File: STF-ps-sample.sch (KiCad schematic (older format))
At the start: 69 parts

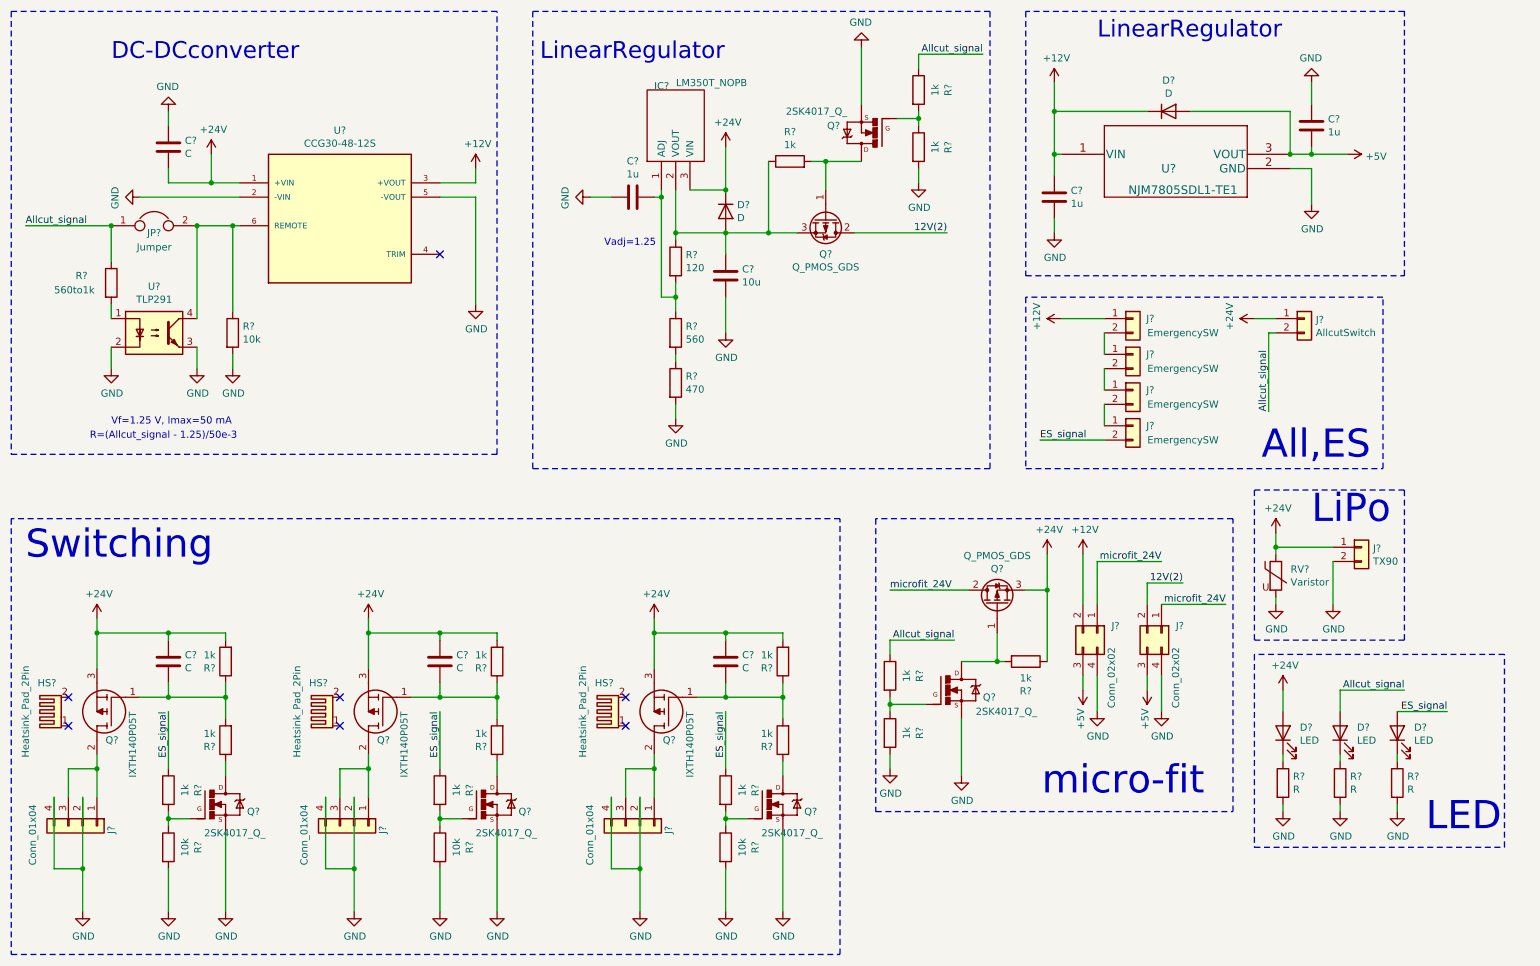
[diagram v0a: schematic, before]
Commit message: just started pcb layout
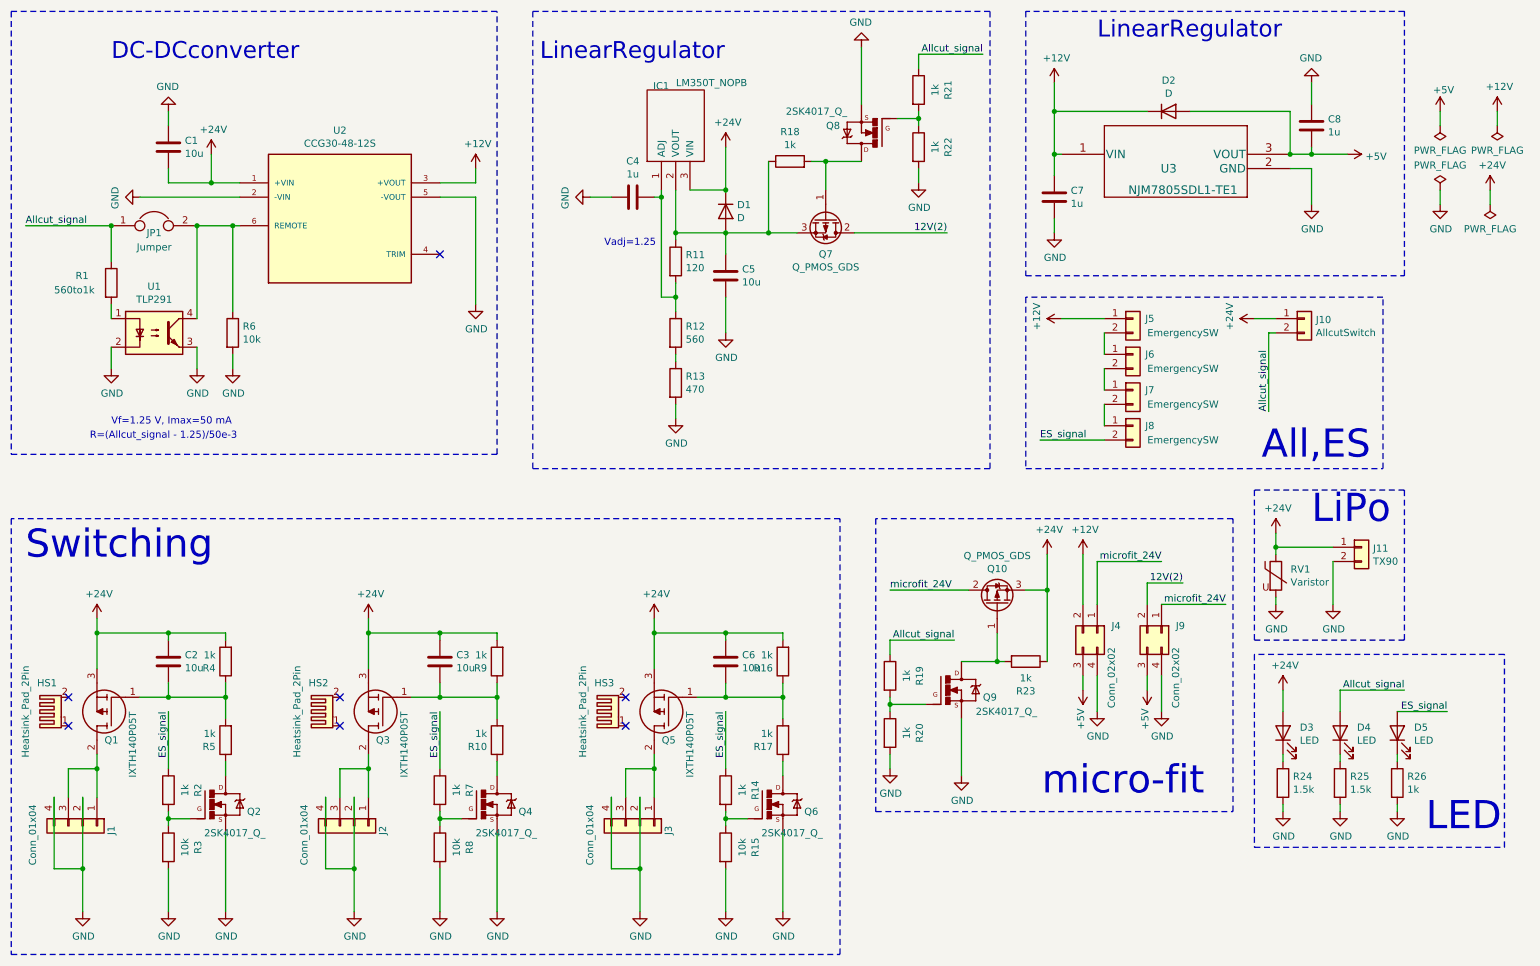
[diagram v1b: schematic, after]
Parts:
- C1, C2, C3, C6: renamed from C?; value C -> 10u; footprint (none) -> Capacitor_THT:C_Disc_D4.3mm_W1.9mm_P5.00mm
- C4, C5, C7, C8: renamed from C?; footprint (none) -> Capacitor_THT:C_Disc_D4.3mm_W1.9mm_P5.00mm
- D1, D2: renamed from D?; footprint (none) -> Diode_THT:D_DO-35_SOD27_P2.54mm_Vertical_AnodeUp
- D3, D4, D5: renamed from D?; footprint (none) -> LED_THT:LED_D3.0mm
- HS1, HS2, HS3: renamed from HS?; footprint (none) -> 00_kicad_mods:stf_01_HeatSink_25x17
- IC1: renamed from IC?; footprint TO254P470X1028X1955-3P -> 00_kicad_mods:stf_03_LM350T
- J1, J2, J3: renamed from J?; footprint (none) -> 00_kicad_mods:stf_08_tanshidai_4P_cover
- J10, J5, J6, J7, J8: renamed from J?; footprint (none) -> Connector_JST:JST_XH_B2B-XH-A_1x02_P2.50mm_Vertical
- J11: renamed from J?; footprint (none) -> 00_kicad_mods:stf_06_XT90PW
- J4, J9: renamed from J?; footprint (none) -> 00_kicad_mods:stf_07_molex_microfit4P_vertical_3Dmodel
- JP1: renamed from JP?; footprint (none) -> Jumper:SolderJumper-2_P1.3mm_Open_TrianglePad1.0x1.5mm
- Q1, Q3, Q5: renamed from Q?; footprint TO545P530X1600X2596-3P -> 00_kicad_mods:stf_02_IXTH140P05T
- Q10, Q7: renamed from Q?; footprint (none) -> 00_kicad_mods:stf_11_TO230P230X650X740-3P
- Q2, Q4, Q6, Q8, Q9: renamed from Q?; footprint TO230P230X650X740-3P -> 00_kicad_mods:stf_11_TO230P230X650X740-3P
- R1, R10, R11, R12, R13, R14, R15, R16, R17, R18, R19, R2, R20, R21, R22, R23, R3, R4, R5, R6, R7, R8, R9: renamed from R?; footprint (none) -> Resistor_THT:R_Axial_DIN0204_L3.6mm_D1.6mm_P5.08mm_Horizontal
- R24, R25: renamed from R?; value R -> 1.5k; footprint (none) -> Resistor_THT:R_Axial_DIN0204_L3.6mm_D1.6mm_P5.08mm_Horizontal
- R26: renamed from R?; value R -> 1k; footprint (none) -> Resistor_THT:R_Axial_DIN0204_L3.6mm_D1.6mm_P5.08mm_Horizontal
- RV1: renamed from RV?; footprint (none) -> Varistor:RV_Disc_D9mm_W3.3mm_P5mm
- U1: renamed from U?; footprint Package_SO:SOIC-4_4.55x2.6mm_P1.27mm -> 00_kicad_mods:stf_05_TLP291_4.55x2.6mm_P1.27mm
- U2: renamed from U?; footprint CCG30-48-12S -> 00_kicad_mods:stf_09_CCG30-48-12S
- U3: renamed from U?; footprint TO-252-3-L1_NMD -> 00_kicad_mods:stf_04_NJM7805SDL1-TE1

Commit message: fnished
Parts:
- R1, R19: footprint Resistor_THT:R_Axial_DIN0204_L3.6mm_D1.6mm_P5.08mm_Horizontal -> Resistor_THT:R_Axial_DIN0204_L3.6mm_D1.6mm_P7.62mm_Horizontal
- R14, R7: footprint Resistor_THT:R_Axial_DIN0204_L3.6mm_D1.6mm_P5.08mm_Horizontal -> Resistor_THT:R_Axial_DIN0207_L6.3mm_D2.5mm_P10.16mm_Horizontal
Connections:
- net ES_signal: now also R26.1; no longer D5.2 (A)
- net GND: now also D5.1 (K); no longer R26.2
- new net: D5.2 (A), R26.2
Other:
- moved on the sheet: D5, R26
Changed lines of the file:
@@
 F 0 "R1" H 1050 2600 50  0000 L CNN
 F 1 "560to1k" H 900 2500 50  0000 L CNN
-F 2 "Resistor_THT:R_Axial_DIN0204_L3.6mm_D1.6mm_P5.08mm_Horizontal" V 1230 2550 50  0001 C CNN
+F 2 "Resistor_THT:R_Axial_DIN0204_L3.6mm_D1.6mm_P7.62mm_Horizontal" V 1230 2550 50  0001 C CNN
 F 3 "~" H 1300 2550 50  0001 C CNN
 	1    1300 2550
@@
 F 0 "R7" V 3807 6100 50  0000 C CNN
 F 1 "1k" V 3716 6100 50  0000 C CNN
-F 2 "Resistor_THT:R_Axial_DIN0204_L3.6mm_D1.6mm_P5.08mm_Horizontal" V 3530 6100 50  0001 C CNN
+F 2 "Resistor_THT:R_Axial_DIN0207_L6.3mm_D2.5mm_P10.16mm_Horizontal" V 3530 6100 50  0001 C CNN
 F 3 "~" H 3600 6100 50  0001 C CNN
 	1    3600 6100
@@
 F 0 "R14" V 5807 6100 50  0000 C CNN
 F 1 "1k" V 5716 6100 50  0000 C CNN
-F 2 "Resistor_THT:R_Axial_DIN0204_L3.6mm_D1.6mm_P5.08mm_Horizontal" V 5530 6100 50  0001 C CNN
+F 2 "Resistor_THT:R_Axial_DIN0207_L6.3mm_D2.5mm_P10.16mm_Horizontal" V 5530 6100 50  0001 C CNN
 F 3 "~" H 5600 6100 50  0001 C CNN
 	1    5600 6100
@@
 F 0 "R19" V 6957 5300 50  0000 C CNN
 F 1 "1k" V 6866 5300 50  0000 C CNN
-F 2 "Resistor_THT:R_Axial_DIN0204_L3.6mm_D1.6mm_P5.08mm_Horizontal" V 6680 5300 50  0001 C CNN
+F 2 "Resistor_THT:R_Axial_DIN0204_L3.6mm_D1.6mm_P7.62mm_Horizontal" V 6680 5300 50  0001 C CNN
 F 3 "~" H 6750 5300 50  0001 C CNN
 	1    6750 5300
@@
 L Device:LED D5
 U 1 1 678E7A5A
-P 10300 5700
-F 0 "D5" V 10339 5582 50  0000 R CNN
-F 1 "LED" V 10248 5582 50  0000 R CNN
-F 2 "LED_THT:LED_D3.0mm" H 10300 5700 50  0001 C CNN
-F 3 "~" H 10300 5700 50  0001 C CNN
-	1    10300 5700
+P 10300 6050
+F 0 "D5" V 10339 5932 50  0000 R CNN
+F 1 "LED" V 10248 5932 50  0000 R CNN
+F 2 "LED_THT:LED_D3.0mm" H 10300 6050 50  0001 C CNN
+F 3 "~" H 10300 6050 50  0001 C CNN
+	1    10300 6050
 	0    -1   -1   0
 $EndComp
@@
 L Device:R R26
 U 1 1 678E935A
-P 10300 6050
-F 0 "R26" H 10370 6096 50  0000 L CNN
-F 1 "1k" H 10370 6005 50  0000 L CNN
-F 2 "Resistor_THT:R_Axial_DIN0204_L3.6mm_D1.6mm_P5.08mm_Horizontal" V 10230 6050 50  0001 C CNN
-F 3 "~" H 10300 6050 50  0001 C CNN
-	1    10300 6050
-	1    0    0    -1
-$EndComp
+P 10300 5700
+F 0 "R26" H 10370 5746 50  0000 L CNN
+F 1 "1k" H 10370 5655 50  0000 L CNN
+F 2 "Resistor_THT:R_Axial_DIN0204_L3.6mm_D1.6mm_P5.08mm_Horizontal" V 10230 5700 50  0001 C CNN
+F 3 "~" H 10300 5700 50  0001 C CNN
+	1    10300 5700
+	1    0    0    -1
+$EndComp
